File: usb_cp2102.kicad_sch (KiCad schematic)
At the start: 21 parts, among them Q4 2N7002, U2 CP2102N-Axx-xQFN28

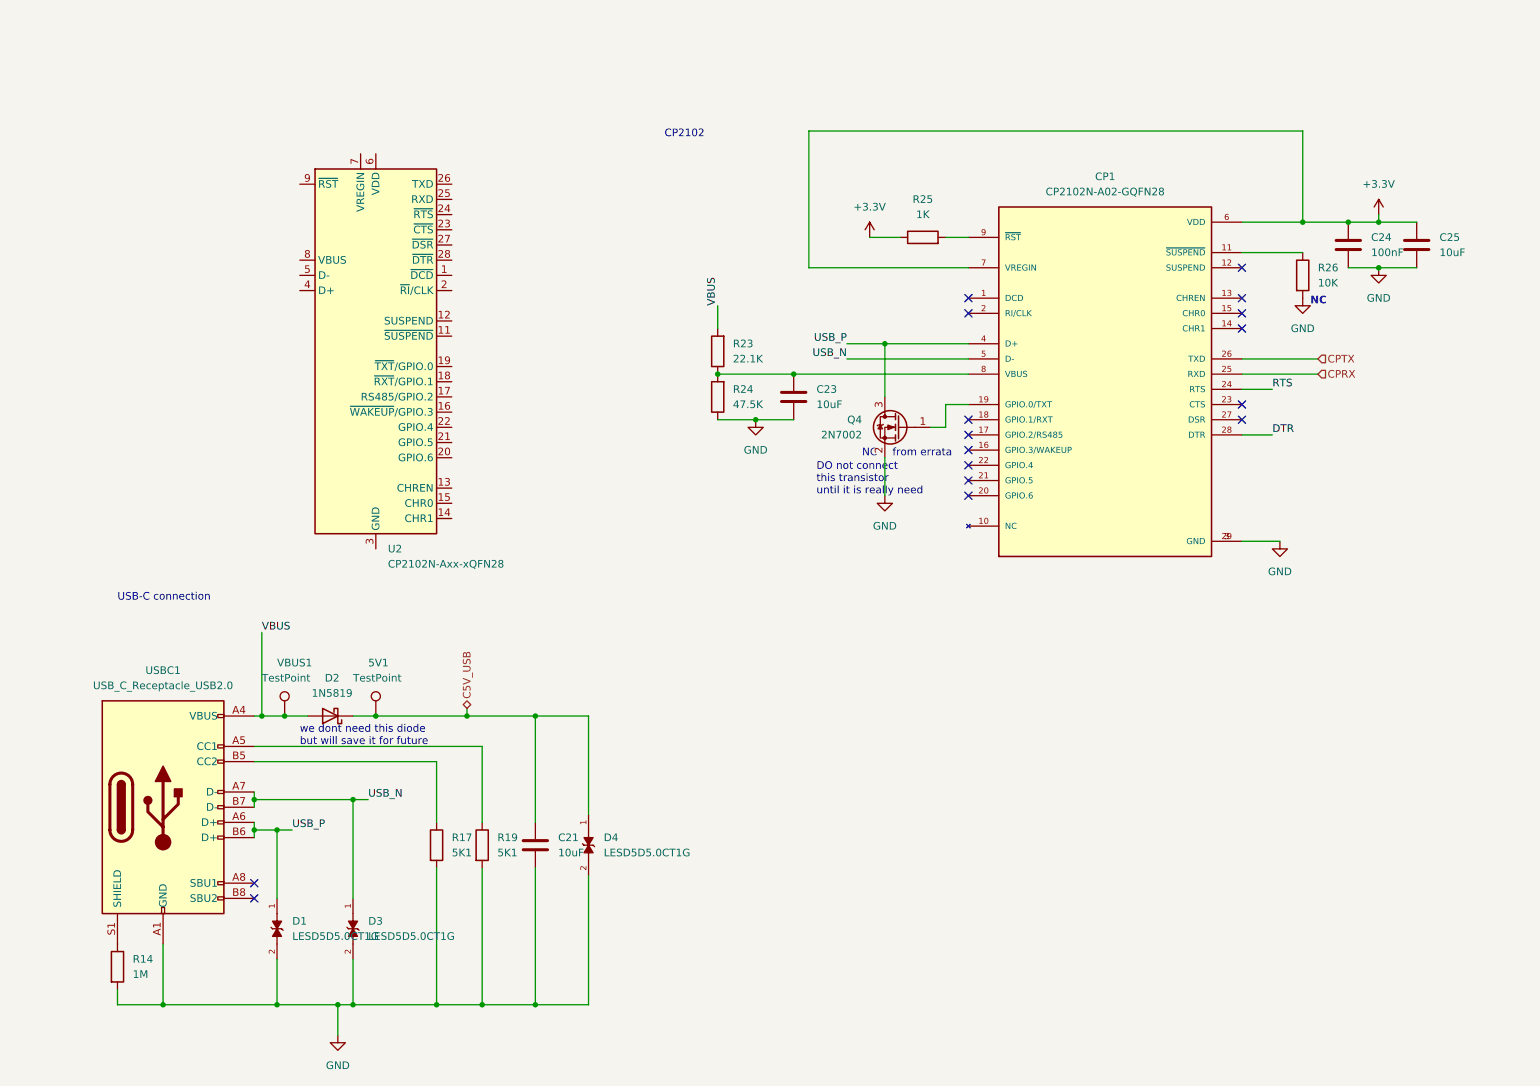
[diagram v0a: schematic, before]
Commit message: added cp2102 schematics
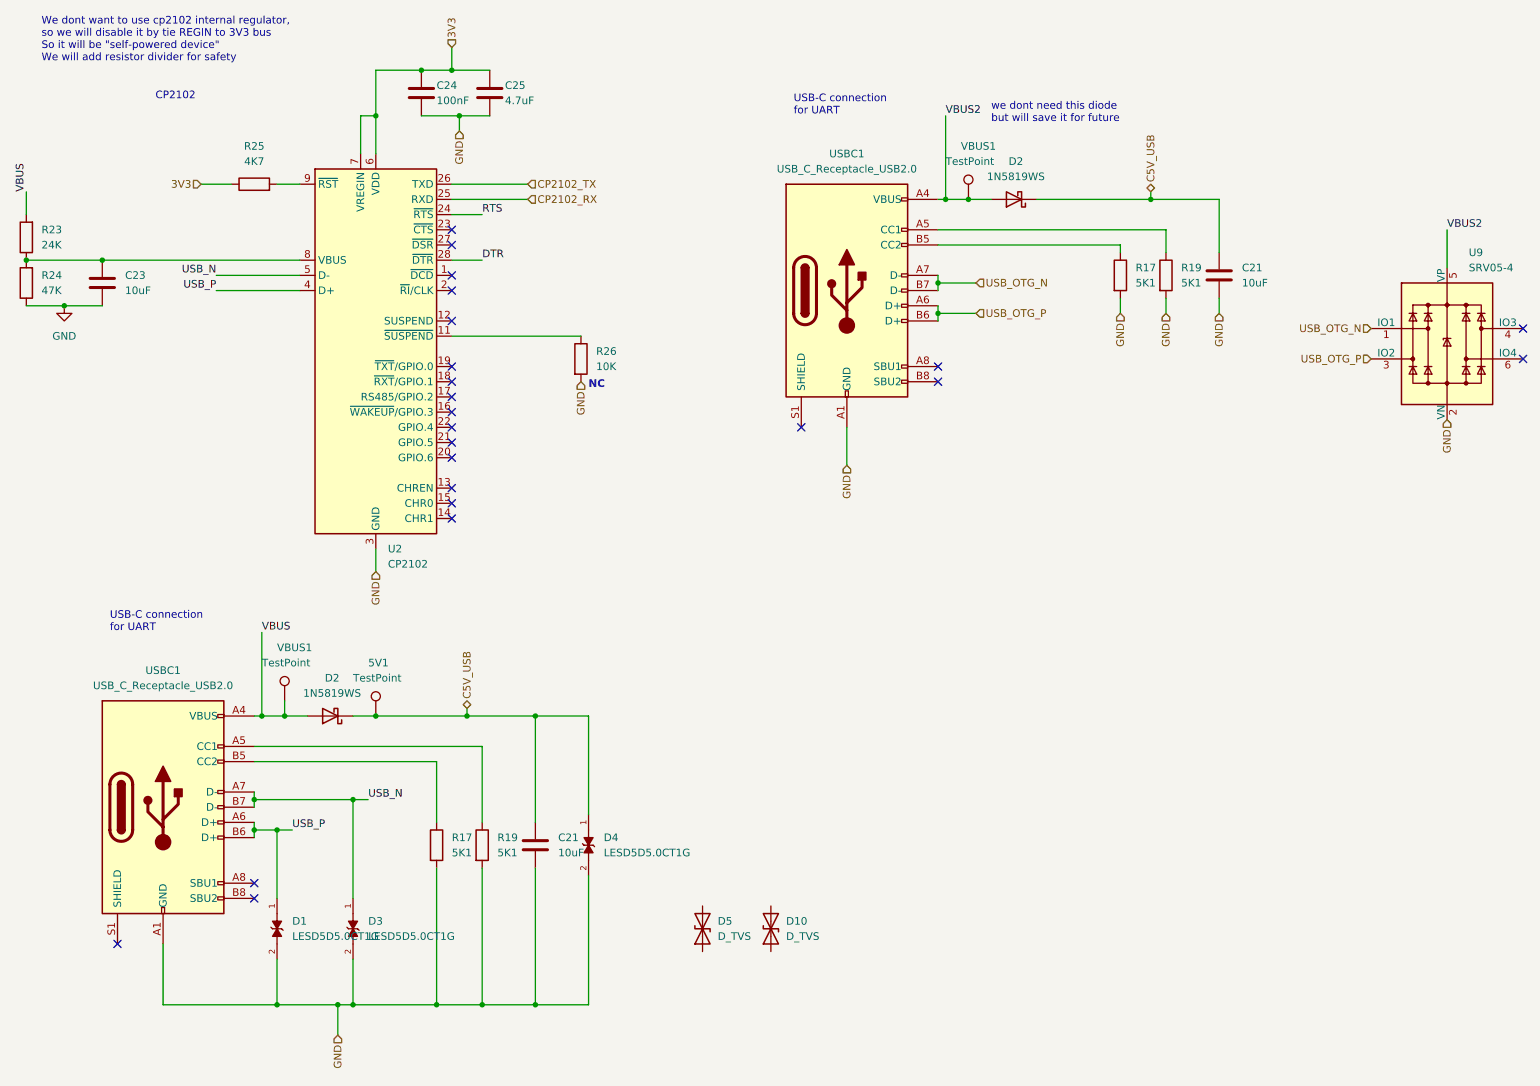
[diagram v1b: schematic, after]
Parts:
- removed CP1: CP2102N-A02-GQFN28, CP2102N-A02-GQFN28:QFN50P500X500X80-29N, symbol CP2102N-A02-GQFN28:CP2102N-A02-GQFN28
- removed Q4: 2N7002, Package_TO_SOT_SMD:SOT-23, symbol Transistor_FET:2N7002
- removed R14: 1M, Resistor_SMD:R_0805_2012Metric, symbol Device:R
- added C21: 10uF, Capacitor_SMD:C_0805_2012Metric, symbol Device:C
- added D10, D5: D_TVS, symbol Device:D_TVS
- added D2: 1N5819WS, Diode_SMD:D_SOD-323, symbol Diode:1N5819
- added R17, R19: 5K1, Resistor_SMD:R_0805_2012Metric, symbol Device:R
- added U9: SRV05-4, Package_TO_SOT_SMD:SOT-23-6, symbol Power_Protection:SRV05-4
- added USBC1: USB_C_Receptacle_USB2.0, Connector_USB:USB_C_Receptacle_HRO_TYPE-C-31-M-12, symbol Connector:USB_C_Receptacle_USB2.0
- added VBUS1: TestPoint, TestPoint:TestPoint_Pad_2.0x2.0mm, symbol Connector:TestPoint
- C25: value 10uF -> 4.7uF
- D2: value 1N5819 -> 1N5819WS; footprint Diode_SMD:D_SMA -> Diode_SMD:D_SOD-323
- R23: value 22.1K -> 24K
- R24: value 47.5K -> 47K
- R25: value 1K -> 4K7
- U2: value CP2102N-Axx-xQFN28 -> CP2102
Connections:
- net +3.3V is gone; now on net 3V3: C24.1, C25.1, R25.1
- net C5V_USB: now also C21.1, D2.1 (K)
- net DTR: now also U2.28 (~{DTR})
- net GND: now also U2.29 (GND), U2.3 (GND), C21.2, R17.2, R19.2, U9.2 (VN), USBC1.A1 (GND), USBC1.A12 (GND), USBC1.B1 (GND), USBC1.B12 (GND)
- net RTS: now also U2.24 (~{RTS})
- net USB_N: now also U2.5 (D-)
- net USB_P: now also U2.4 (D+)
- net at C23.1, R23.1, R24.2: now also U2.8 (VBUS)
- net at R26.1: now also U2.11 (~{SUSPEND})
- net at R25.2: now also U2.9 (~{RST})
- net CP2102_RX: now reaches U2.25 (RXD)
- net CP2102_TX: now reaches U2.26 (TXD)
- net 3V3: now reaches U2.6 (VDD)
- net 3V3: now also U2.7 (VREGIN)
- new net: R19.1, USBC1.A5 (CC1)
- new net: R17.1, USBC1.B5 (CC2)
- new net USB_OTG_N: U9.1 (IO1), USBC1.A7 (D-), USBC1.B7 (D-)
- new net USB_OTG_P: U9.3 (IO2), USBC1.A6 (D+), USBC1.B6 (D+)
- new net VBUS2: D2.2 (A), U9.5 (VP), USBC1.A4 (VBUS), USBC1.A9 (VBUS), USBC1.B4 (VBUS), USBC1.B9 (VBUS), VBUS1.1
- no-connect marks 16 -> 23
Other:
- note added: "USB-C connection for UART"
- note added: "We dont want to use cp2102 internal regulator, so we will disable it by tie REGIN to 3V3 bus So it will be "self-powered device" We will add resistor divider for safety"
- note removed: "DO not connect this transistor until it is really need"
- note removed: "USB-C connection"
- note removed: "from errata"
- moved on the sheet: VBUS1

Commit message: schematics almost finished
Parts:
- removed D1, D3, D4: LESD5D5.0CT1G, LESD5D5:TVS_LESD5D5.0CT1G, symbol LESD5D5.0CT1G:LESD5D5.0CT1G
- removed D10, D5: D_TVS, symbol Device:D_TVS
- removed D2 (x2): 1N5819WS, Diode_SMD:D_SOD-323, symbol Diode:1N5819
- added D1, D3, D4: H5VL10B, PMEG2005AEL_315:DIODFN2_98X58X50L26X51N, symbol Device:D_TVS
- added D2: SS54, Diode_SMD:D_SMA, symbol Diode:1N5819
- added H1, H2, H3, H4: MountingHole, MountingHole:MountingHole_3.2mm_M3, symbol Mechanical:MountingHole
- C23: renamed from C21; now left out of the parts list
- R24: renamed from R17; now left out of the parts list
- R25: renamed from R19; now left out of the parts list
- U9: now left out of the parts list
- USBC2: renamed from USBC1; now left out of the parts list
- renumbered C24 to C26, C25 to C27, C23 to C28, R25 to R31, R26 to R32, R23 to R33, R24 to R34, VBUS1 to VBUS2
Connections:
- net VBUS is gone; now on net C5V_USB: R33.2, USBC1.A4 (VBUS), USBC1.A9 (VBUS), USBC1.B4 (VBUS), USBC1.B9 (VBUS), VBUS1.1
- net VBUS2 is gone; now on net C5V_USB: U9.5 (VP), USBC2.A4 (VBUS), USBC2.A9 (VBUS), USBC2.B4 (VBUS), USBC2.B9 (VBUS), VBUS2.1
- net C5V_USB: now also D4.2 (A2)
- net GND: now also D1.1 (A1), D3.1 (A1), D4.1 (A1)
- net USB_N: now also D1.2 (A2)
- net USB_P: now also D3.2 (A2)
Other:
- note added: "There can be schottky diode between usb 5v and 5v power rail, but now we do not need it because it is already in power selector scheme"
- note added: "USB-C connection for USB-HID"
- note added: "USB-OTG connector temporally removed from pcb"
- note removed: "we dont need this diode but will save it for future"
- moved on the sheet: U9

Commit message: pre pre production
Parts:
- removed H4: MountingHole, MountingHole:MountingHole_3.2mm_M3, symbol Mechanical:MountingHole
- removed VBUS1: TestPoint, TestPoint:TestPoint_Pad_2.0x2.0mm, symbol Connector:TestPoint
- added C36: 5uF, Capacitor_SMD:C_0805_2012Metric, symbol Device:C
- 5V1: footprint TestPoint:TestPoint_Pad_2.0x2.0mm -> TestPoint:TestPoint_Pad_1.0x1.0mm
- C21: value 10uF -> 5uF
- H1, H2, H3: footprint MountingHole:MountingHole_3.2mm_M3 -> MountingHole:MountingHole_2.7mm_M2.5_ISO7380
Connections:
- net C5V_USB: now also C36.1
- net GND: now also C36.2
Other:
- moved on the sheet: D4
